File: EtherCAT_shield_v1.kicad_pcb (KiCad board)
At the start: 2 copper layers, 69 parts, among them J1 RJ45-TRANSFO, J2 RJ45-TRANSFO, P1 CONN_02X10, P2 CONN_02X19, P3 CONN_02X19, U1 LAN9252, U2 24LC00, Y1 Crystal_GND24

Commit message: ピンソケットの位置合わせ
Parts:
- moved R1 81.6 mm to (98.9, 61.0)
- moved R2 81.6 mm to (101.9, 61.0)
- moved R3 81.6 mm to (104.8, 61.0)
- moved C1 72.5 mm to (59.0, 62.3)
- moved C10 72.5 mm to (153.4, 32.7)
- moved C12 72.5 mm to (138.2, 53.8)
- moved C13 72.5 mm to (150.2, 37.8)
- moved C17 72.5 mm to (160.7, 32.7)
- moved C18 72.5 mm to (164.4, 32.7)
- moved C2 72.5 mm to (54.3, 67.3)
- moved C20 72.5 mm to (157.2, 37.8)
- moved C21 72.5 mm to (149.8, 42.8)
- moved C23 72.5 mm to (145.1, 49.8)
- moved C24 72.5 mm to (141.5, 53.8)
- moved C25 72.5 mm to (160.7, 37.8)
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
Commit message: 適当に外形起こした
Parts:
- moved C10 118.4 mm to (134.3, 149.6)
- moved C11 118.4 mm to (127.3, 156.5)
- moved C12 118.4 mm to (119.2, 170.6)
- moved C13 118.4 mm to (131.2, 154.6)
- moved C14 118.4 mm to (127.3, 161.6)
- moved C15 118.4 mm to (138.0, 149.6)
- moved C16 118.4 mm to (122.6, 165.6)
- moved C17 118.4 mm to (141.7, 149.6)
- moved C18 118.4 mm to (145.4, 149.6)
- moved C19 118.4 mm to (139.7, 164.7)
- moved C2 118.4 mm to (35.3, 184.2)
- moved C20 118.4 mm to (138.2, 154.6)
- moved C23 118.4 mm to (126.1, 166.6)
- moved C24 118.4 mm to (122.5, 170.6)
- moved C25 118.4 mm to (141.7, 154.6)
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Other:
- board outline added: 73.7 x 81.3 mm

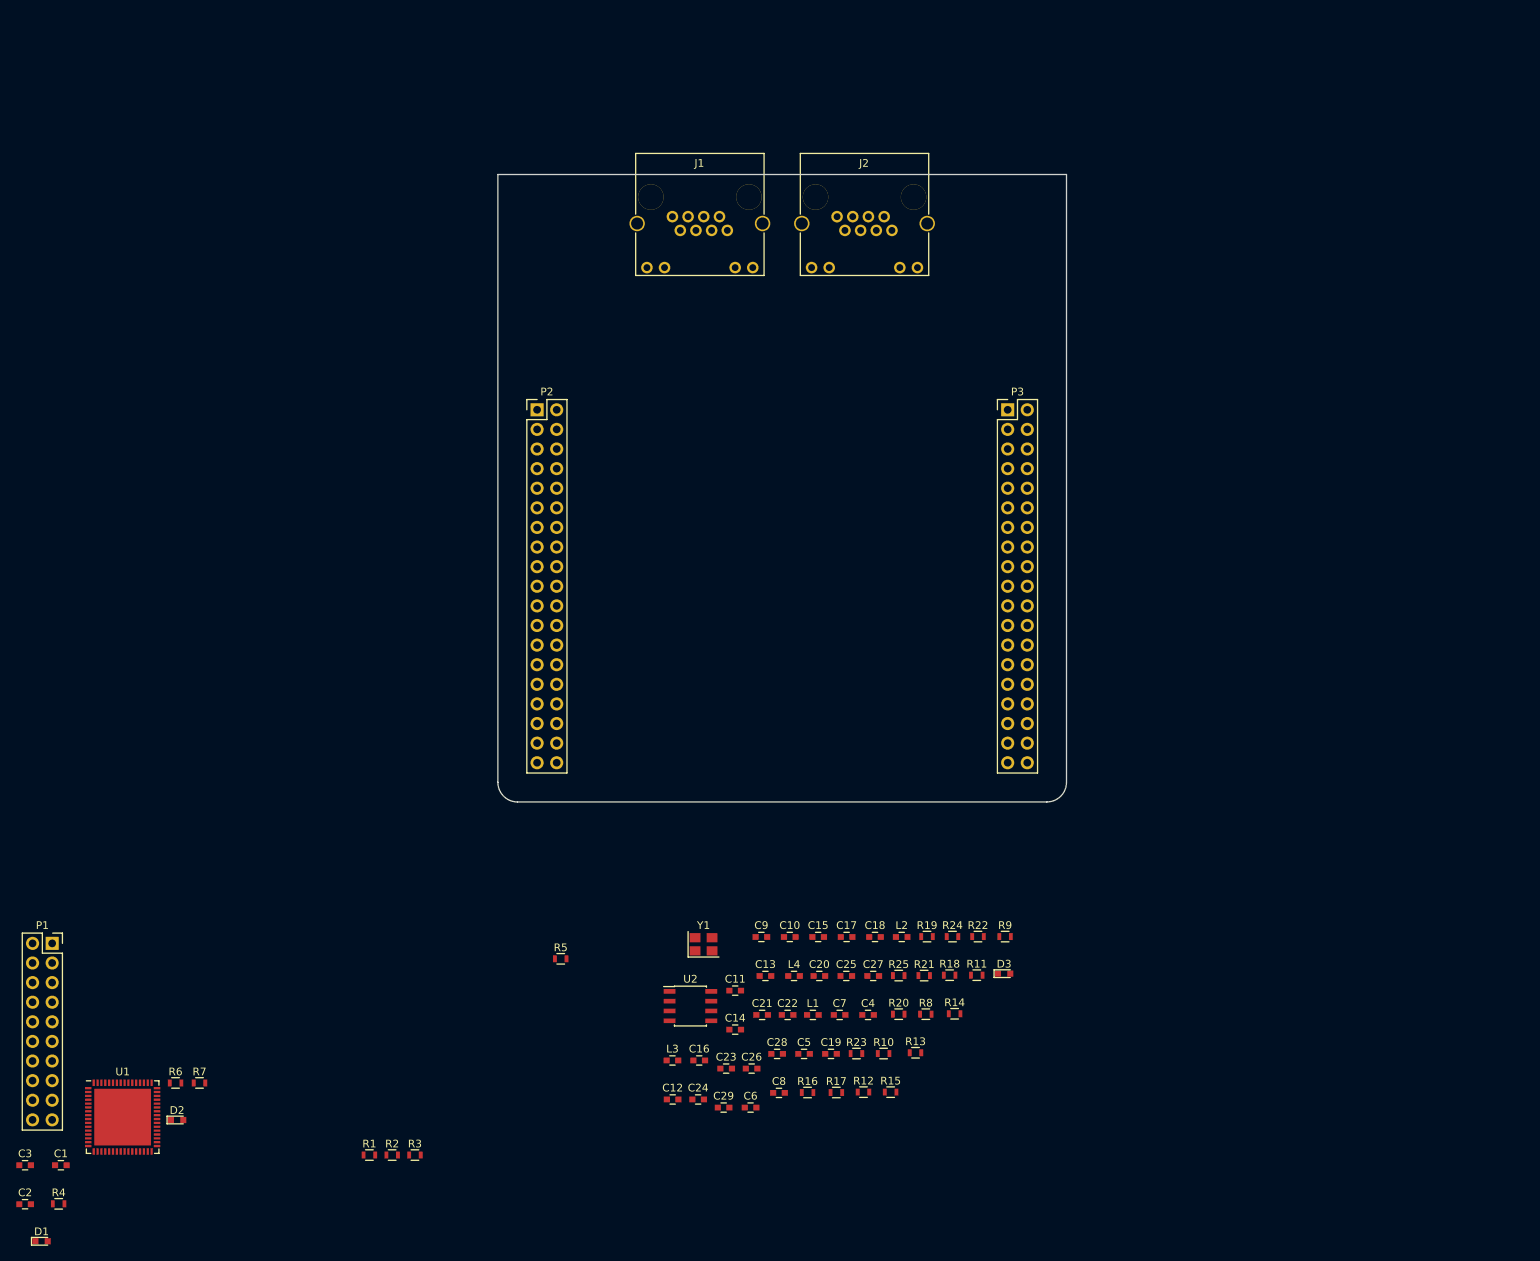
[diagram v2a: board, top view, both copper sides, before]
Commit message: 部品変更，再アノテーション，コネクタだけ配置
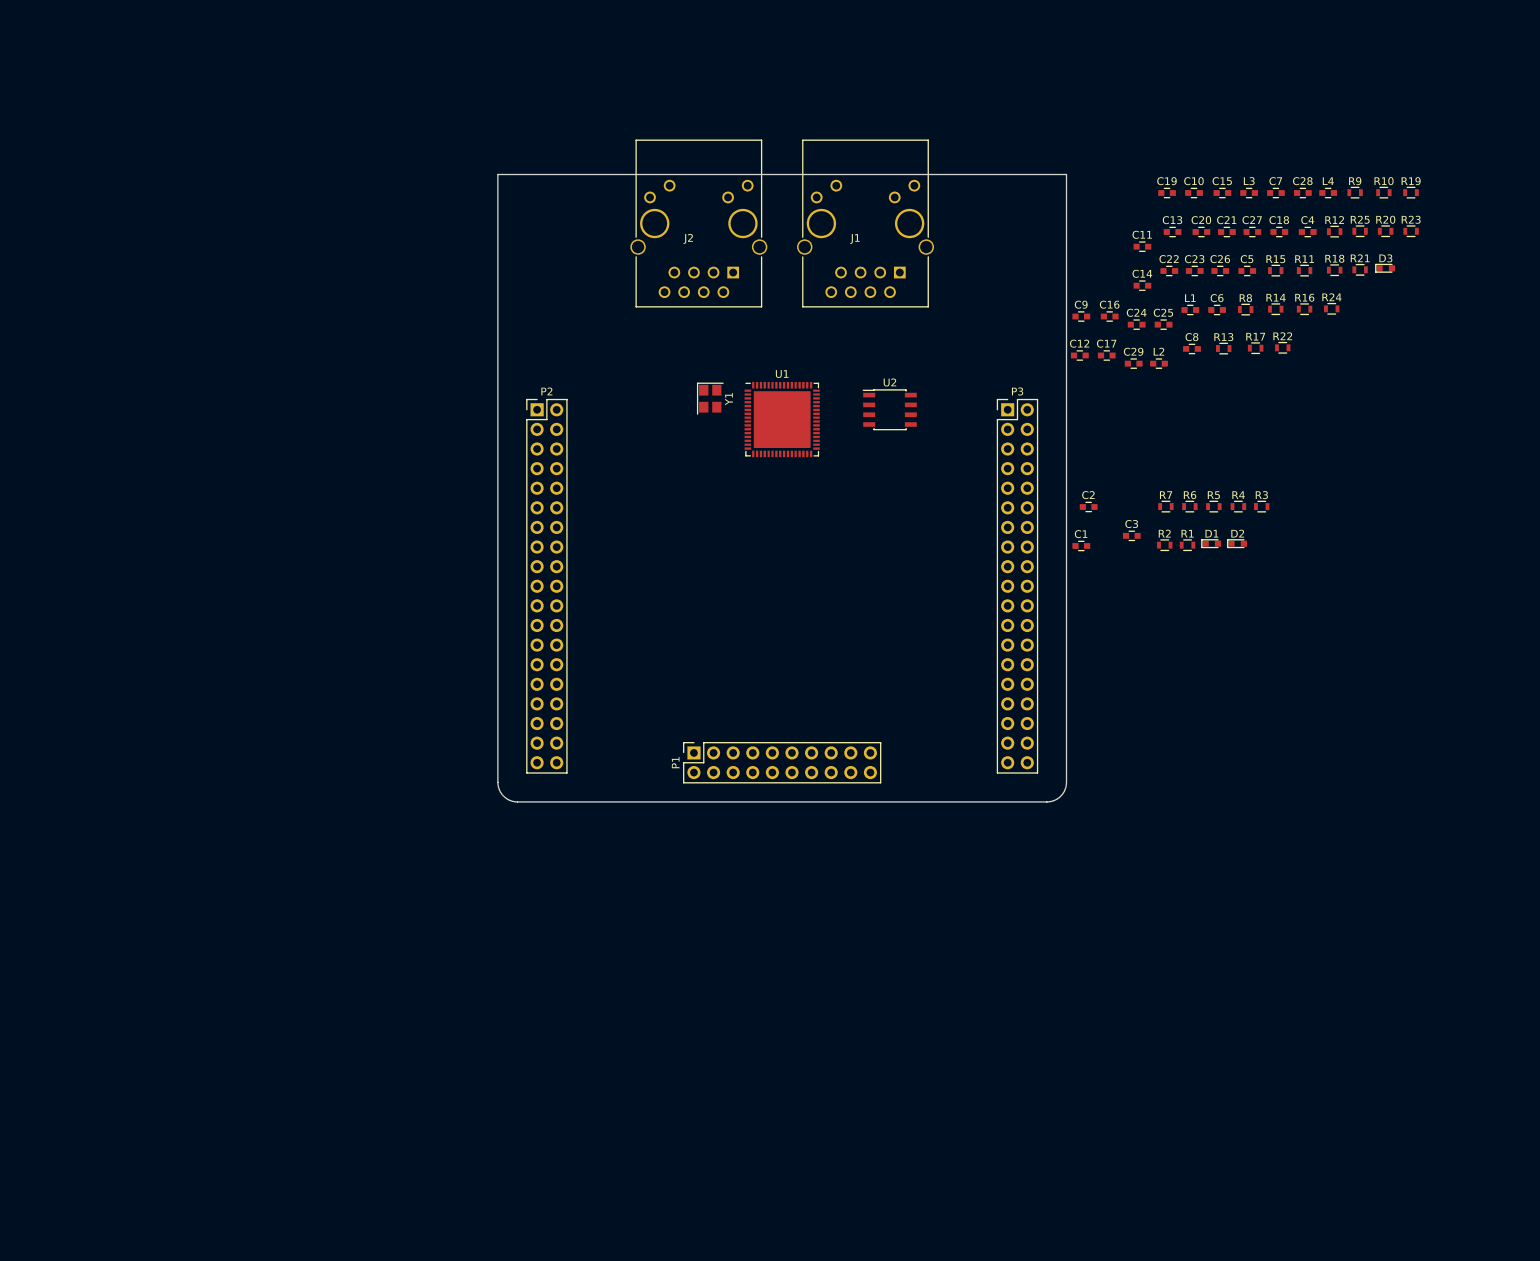
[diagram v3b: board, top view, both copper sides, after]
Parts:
- J1, J2: value RJ45-TRANSFO -> RJ45-PULSETRANS; footprint Connect:RJHSE538X -> Connect:RJ45_J0011D21BNL
- moved R4 177.5 mm to (192.4, 93.8)
- moved D1 176.5 mm to (189.0, 98.6)
- moved C3 164.9 mm to (178.6, 97.6)
- moved C2 164.7 mm to (173.1, 93.9)
- moved D2 156.4 mm to (192.4, 98.6)
- moved C1 154.6 mm to (172.1, 98.9)
- moved R6 151.1 mm to (186.2, 93.8)
- moved R7 145.8 mm to (183.1, 93.8)
- moved R3 138.2 mm to (195.5, 93.8)
- moved L3 134.9 mm to (193.8, 53.2)
- moved R1 132.2 mm to (185.9, 98.8)
- moved C28 130.7 mm to (200.8, 53.2)
- moved R10 129.0 mm to (211.3, 53.1)
- moved R23 128.5 mm to (214.8, 58.1)
- moved R2 127.5 mm to (182.9, 98.8)
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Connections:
- J1 pad 10: (no net) -> GND
- J1 pad 2: Net-(C2-Pad1) -> /LAN9252/TXNA
- J1 pad 3: /LAN9252/TXNA -> /LAN9252/RXPA
- J1 pad 4: /LAN9252/RXPA -> Net-(C2-Pad1)
- J1 pad 9: (no net) -> Net-(J1-Pad9)
- J2 pad 10: (no net) -> GND
- J2 pad 2: Net-(C3-Pad1) -> /LAN9252/TXNB
- J2 pad 3: /LAN9252/TXNB -> /LAN9252/RXPB
- J2 pad 4: /LAN9252/RXPB -> Net-(C3-Pad1)
- J2 pad 9: (no net) -> Net-(J2-Pad9)
- R5 pad 2: (no net) -> Net-(J1-Pad9)
- R7 pad 2: (no net) -> Net-(J2-Pad9)

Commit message: 進捗
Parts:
- C12, C13, C14, C15, C16, C17, C18, L3, R13, R24, R25, R5, R7: moved to B.Cu
- moved R10 78.3 mm to (136.2, 75.5), turned to 90 degrees
- moved C28 73.5 mm to (129.1, 69.3), turned to 180 degrees
- moved R9 72.9 mm to (138.2, 75.5), turned to 90 degrees
- moved R14 71.1 mm to (126.5, 75.5), turned to 90 degrees
- moved C20 71.0 mm to (121.7, 84.5), turned to 90 degrees
- moved R16 70.9 mm to (130.4, 75.5), turned to 90 degrees
- moved C18 70.3 mm to (131.4, 81.5), turned to 180 degrees
- moved R15 69.9 mm to (128.5, 75.5), turned to 90 degrees
- moved C27 68.8 mm to (126.3, 69.3)
- moved L3 68.0 mm to (130.8, 78.7), turned to 270 degrees
- moved R11 67.8 mm to (134.3, 75.5), turned to 90 degrees
- moved C19 67.7 mm to (121.7, 81.5), turned to 270 degrees
- moved C26 66.9 mm to (123.5, 69.3), turned to 180 degrees
- moved R7 66.2 mm to (131.5, 52.2), turned to 180 degrees
- moved C3 63.5 mm to (121.4, 70.0), turned to 270 degrees
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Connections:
- net /LAN9252/RXNA renamed RX1_N
- net /LAN9252/RXNB renamed RX2_N
- net /LAN9252/RXPA renamed RX1_P
- net /LAN9252/RXPB renamed RX2_P
- net /LAN9252/TXNA renamed TX1_N
- net /LAN9252/TXNB renamed TX2_N
- net /LAN9252/TXPA renamed TX1_P
- net /LAN9252/TXPB renamed TX2_P
- C16 pad 1: /LAN9252/VDDTXRX2 -> Net-(C16-Pad1)
- C18 pad 1: /LAN9252/VDD33TXRX1 -> Net-(C16-Pad1)
- L4 pad 2: Net-(L4-Pad2) -> Net-(C16-Pad1)
- U1 pad 56: Net-(L4-Pad2) -> Net-(C16-Pad1)
- U1 pad 59: Net-(L4-Pad2) -> Net-(C16-Pad1)
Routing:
- net GND: track 0.00 -> 87.9 mm, vias 0 -> 12
- net /LAN9252/LINKACTLED1: track 0.00 -> 58.3 mm, vias 0 -> 1
- net TX1_N: track 0.00 -> 39.4 mm
- net TX1_P: track 0.00 -> 39.3 mm
- net /LAN9252/LINKACTLED0: track 0.00 -> 39.2 mm, vias 0 -> 1
- net RX2_P: track 0.00 -> 32.8 mm
- net RX2_N: track 0.00 -> 32.7 mm
- net RX1_P: track 0.00 -> 28.2 mm
- net RX1_N: track 0.00 -> 28.2 mm
- net TX2_P: track 0.00 -> 24.7 mm
- net TX2_N: track 0.00 -> 24.3 mm
- net /LAN9252/VDD33TXRX1: track 0.00 -> 19.1 mm, vias 0 -> 4
- net /LAN9252/VDDTXRX2: track 0.00 -> 18.5 mm, vias 0 -> 4
- net Net-(C20-Pad1): track 0.00 -> 10.6 mm
- net Net-(C19-Pad1): track 0.00 -> 8.62 mm
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
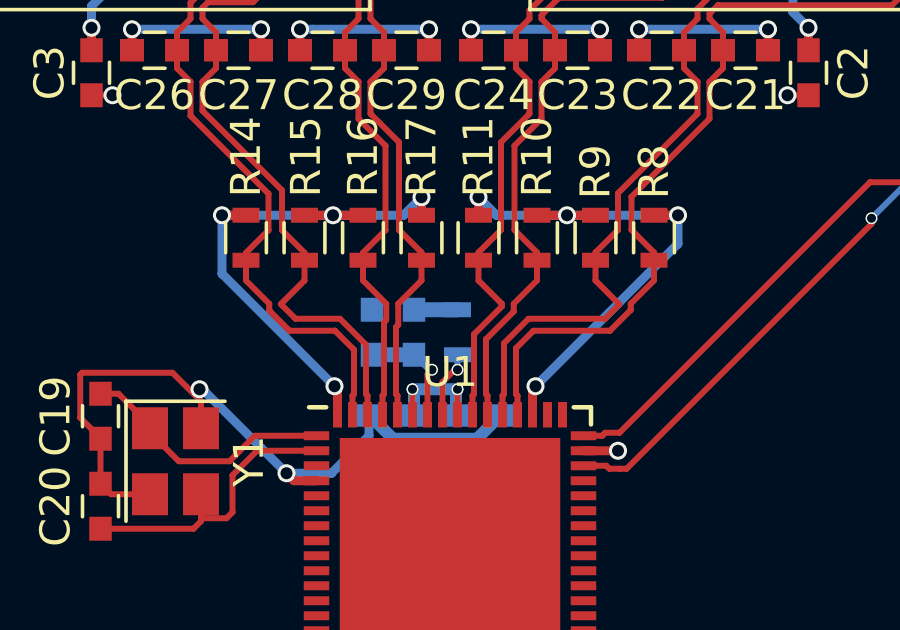
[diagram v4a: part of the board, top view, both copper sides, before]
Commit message: 差動線修正
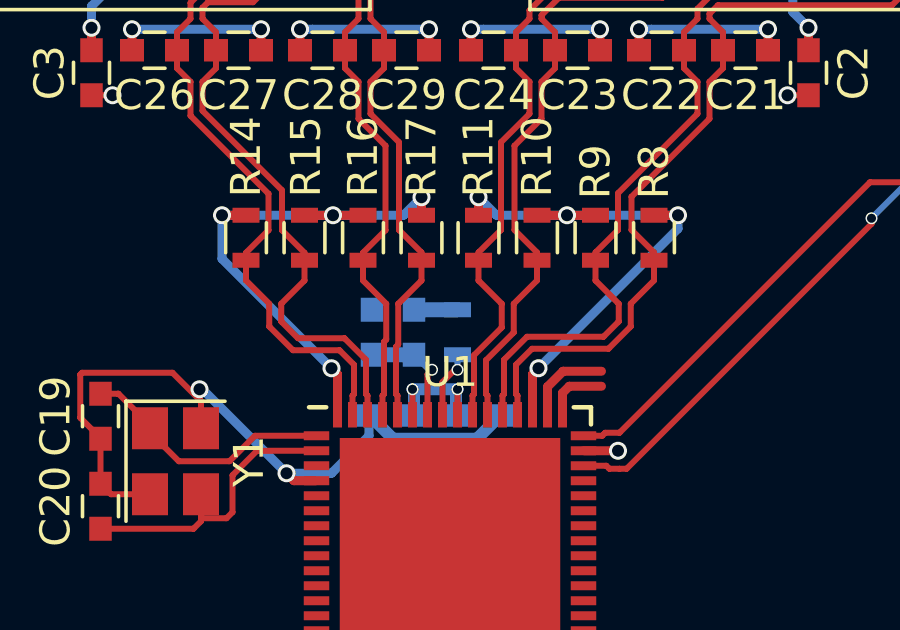
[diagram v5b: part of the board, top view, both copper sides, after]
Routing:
- net Net-(P3-Pad17): track 0.00 -> 2.95 mm
- net Net-(P1-Pad9): track 0.00 -> 2.12 mm

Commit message: 進捗
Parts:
- C11, C4, L1, L2, L4, R3, R6: moved to B.Cu
- moved D2 94.5 mm to (103.1, 67.5), turned to 180 degrees
- moved D1 92.4 mm to (103.1, 64.5), turned to 180 degrees
- moved R1 92.4 mm to (100.1, 64.5)
- moved R2 88.5 mm to (100.1, 67.5)
- moved R21 88.5 mm to (124.8, 92.8), turned to 180 degrees
- moved R12 86.7 mm to (124.8, 91.3), turned to 180 degrees
- moved R18 80.8 mm to (126.9, 84.2), turned to 180 degrees
- moved L4 73.1 mm to (135.1, 77.2), turned to 270 degrees
- moved R4 71.0 mm to (121.6, 89.2)
- moved R6 68.2 mm to (121.4, 72.3), turned to 180 degrees
- moved R19 63.7 mm to (158.4, 82.8), turned to 180 degrees
- moved R20 59.2 mm to (158.4, 84.4), turned to 180 degrees
- moved C11 58.3 mm to (123.4, 74.1), turned to 270 degrees
- moved L2 57.4 mm to (124.8, 74.1), turned to 90 degrees
- moved R23 53.9 mm to (161.0, 56.0), turned to 180 degrees
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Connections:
- J1 pad 11: (no net) -> Net-(J1-Pad11)
- J1 pad 12: (no net) -> Net-(J1-Pad12)
- J1 pad 14: (no net) -> GND
- J2 pad 11: (no net) -> Net-(J2-Pad11)
- J2 pad 12: (no net) -> Net-(J2-Pad12)
- J2 pad 14: (no net) -> GND
- P2 pad 10: (no net) -> Net-(P2-Pad10)
- P2 pad 11: (no net) -> Net-(P2-Pad11)
- P2 pad 13: (no net) -> Net-(P2-Pad13)
- P2 pad 14: (no net) -> Net-(P2-Pad14)
- P2 pad 15: (no net) -> Net-(P2-Pad15)
- P2 pad 17: (no net) -> Net-(P2-Pad17)
- P2 pad 18: (no net) -> Net-(P2-Pad18)
- P2 pad 2: (no net) -> Net-(P2-Pad2)
- P2 pad 21: (no net) -> Net-(P2-Pad21)
- P2 pad 23: (no net) -> Net-(P2-Pad23)
- P2 pad 24: (no net) -> Net-(P2-Pad24)
- P2 pad 25: (no net) -> Net-(P2-Pad25)
- P2 pad 26: (no net) -> Net-(P2-Pad26)
- P2 pad 27: (no net) -> Net-(P2-Pad27)
- P2 pad 28: (no net) -> Net-(P2-Pad28)
- P2 pad 29: (no net) -> Net-(P2-Pad29)
- P2 pad 3: (no net) -> Net-(P2-Pad3)
- P2 pad 30: (no net) -> Net-(P2-Pad30)
- P2 pad 31: (no net) -> Net-(P2-Pad31)
- P2 pad 32: (no net) -> Net-(P2-Pad32)
- P2 pad 33: (no net) -> Net-(P2-Pad33)
- P2 pad 34: (no net) -> Net-(P2-Pad34)
- P2 pad 35: (no net) -> Net-(P2-Pad35)
- P2 pad 36: (no net) -> Net-(P2-Pad36)
- P2 pad 37: (no net) -> Net-(P2-Pad37)
- P2 pad 38: (no net) -> Net-(P2-Pad38)
- P2 pad 4: (no net) -> Net-(P2-Pad4)
- P2 pad 5: (no net) -> Net-(P2-Pad5)
- P2 pad 6: (no net) -> Net-(P2-Pad6)
- P2 pad 7: (no net) -> Net-(P2-Pad7)
- P2 pad 9: (no net) -> Net-(P2-Pad9)
- P3 pad 10: (no net) -> Net-(P3-Pad10)
- P3 pad 11: (no net) -> Net-(P3-Pad11)
- P3 pad 12: (no net) -> Net-(P3-Pad12)
- P3 pad 13: (no net) -> Net-(P3-Pad13)
- P3 pad 14: (no net) -> Net-(P3-Pad14)
- P3 pad 15: (no net) -> Net-(P3-Pad15)
- P3 pad 16: (no net) -> Net-(P3-Pad16)
- P3 pad 18: (no net) -> Net-(P3-Pad18)
- P3 pad 19: (no net) -> Net-(P3-Pad19)
- P3 pad 2: (no net) -> Net-(P3-Pad2)
- P3 pad 21: (no net) -> Net-(P3-Pad21)
- P3 pad 23: (no net) -> Net-(P3-Pad23)
- P3 pad 24: (no net) -> Net-(P3-Pad24)
- P3 pad 25: (no net) -> Net-(P3-Pad25)
- P3 pad 26: (no net) -> Net-(P3-Pad26)
- P3 pad 27: (no net) -> Net-(P3-Pad27)
- P3 pad 28: (no net) -> Net-(P3-Pad28)
- P3 pad 29: (no net) -> Net-(P3-Pad29)
- P3 pad 3: (no net) -> Net-(P3-Pad3)
- P3 pad 30: (no net) -> Net-(P3-Pad30)
- P3 pad 31: (no net) -> Net-(P3-Pad31)
- P3 pad 33: (no net) -> Net-(P3-Pad33)
- P3 pad 34: (no net) -> Net-(P3-Pad34)
- P3 pad 35: (no net) -> Net-(P3-Pad35)
- P3 pad 36: (no net) -> Net-(P3-Pad36)
- P3 pad 37: (no net) -> Net-(P3-Pad37)
- P3 pad 38: (no net) -> Net-(P3-Pad38)
- P3 pad 4: (no net) -> Net-(P3-Pad4)
- P3 pad 5: (no net) -> Net-(P3-Pad5)
- P3 pad 6: (no net) -> Net-(P3-Pad6)
- P3 pad 7: (no net) -> Net-(P3-Pad7)
- P3 pad 8: (no net) -> Net-(P3-Pad8)
- U1 pad 12: (no net) -> Net-(U1-Pad12)
- U1 pad 18: (no net) -> Net-(U1-Pad18)
- U1 pad 25: (no net) -> Net-(U1-Pad25)
- U1 pad 3: (no net) -> Net-(U1-Pad3)
- U1 pad 34: (no net) -> Net-(U1-Pad34)
- U1 pad 35: (no net) -> Net-(U1-Pad35)
- U1 pad 44: (no net) -> /LAN9252/IRQ
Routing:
- net GND: track 87.9 -> 102.6 mm
- net Net-(C16-Pad1): track 4.99 -> 7.39 mm
- net RX2_N: track 32.7 -> 31.2 mm
- net RX2_P: track 32.8 -> 31.4 mm
- net RX1_P: track 28.2 -> 26.8 mm
- net RX1_N: track 28.2 -> 26.8 mm
- net /LAN9252/VDD33TXRX1: track 19.1 -> 20.3 mm, vias 4 -> 3
- net /LAN9252/VDDTXRX2: track 18.5 -> 19.2 mm, vias 4 -> 3
- net TX2_P: track 24.7 -> 24.1 mm
- net TX2_N: track 24.3 -> 23.7 mm
- net TX1_N: track 39.4 -> 38.8 mm
- net TX1_P: track 39.3 -> 38.7 mm
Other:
- board text added: "+3V3"
- board text added: "+5V"
- board text added: "RUN"
